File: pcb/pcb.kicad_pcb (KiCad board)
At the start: 2 copper layers, 100 x 80 mm, 20 parts, among them K1 Generic_Relay, K2 Generic_Relay, Q1 BC547, Q2 BC547

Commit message: Update optocoupler footprint and PCB with new model
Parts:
- OP1: value Optocoupler_L -> Optocoupler_Left; footprint Custom_Footprints:Optocoupler_L -> Custom_Footprints:Optocoupler_Left
- OP2: value Optocoupler_R -> Optocoupler_Right; footprint Custom_Footprints:Optocoupler_R -> Custom_Footprints:Optocoupler_Right
- moved OP2 1.60 mm to (151.2, 65.7)
- moved OP1 1.60 mm to (128.9, 65.7)
- moved R1 0.64 mm to (111.8, 59.7)
- moved R2 0.64 mm to (168.3, 59.7)
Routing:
- net Net-(OP1-LDR1): track 82.8 -> 80.5 mm
- net Net-(OP2-IN1): track 4.44 -> 5.72 mm
- net Net-(Device2-Pin_1): track 24.1 -> 25.4 mm
- net Net-(OP1-IN1): track 4.44 -> 5.71 mm
- net Net-(Device1-Pin_1): track 24.1 -> 25.4 mm
- net Net-(MCU1-D5): track 42.9 -> 43.9 mm
- net Net-(MCU1-D1): track 36.8 -> 37.8 mm
- net Net-(Device2-Pin_3): track 49.1 -> 49.8 mm
- net Net-(Device1-Pin_3): track 34.6 -> 35.2 mm

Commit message: Add PCB mounting holes
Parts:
- added REF**: MountingHole_4mm, MountingHole:MountingHole_4mm, F.Cu at (161.9, 76.2)
- added REF**: MountingHole_4mm, MountingHole:MountingHole_4mm, F.Cu at (97.2, 109.9)
- added REF**: MountingHole_4mm, MountingHole:MountingHole_4mm, F.Cu at (177.2, 118.1)
- added REF**: MountingHole_4mm, MountingHole:MountingHole_4mm, F.Cu at (118.7, 76.2)
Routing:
- net Net-(D3-K): track 146.4 -> 147.5 mm
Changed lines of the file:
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@@
     )
+  )
+  (footprint "MountingHole:MountingHole_4mm" (layer "F.Cu")
+    (at 161.925 76.2)
+    (descr "Mounting Hole 4mm, no annular")
+    (tags "mounting hole 4mm no annular")
+    (attr exclude_from_pos_files exclude_from_bom)
+    (fp_text reference "REF**" (at 0 -5) (layer "F.SilkS") hide
+        (effects (font (size 1 1) (thickness 0.15)))
+    )
+    (fp_text value "MountingHole_4mm" (at 0 5) (layer "F.Fab") hide
+        (effects (font (size 1 1) (thickness 0.15)))
+    )
+    (fp_text user "${REFERENCE}" (at 0 0) (layer "F.Fab")
+        (effects (font (size 1 1) (thickness 0.15)))
+    )
+    (fp_circle (center 0 0) (end 4 0)
+      (stroke (width 0.15) (type solid)) (fill none) (layer "Cmts.User"))
+    (fp_circle (center 0 0) (end 4.25 0)
+      (stroke (width 0.05) (type solid)) (fill none) (layer "F.CrtYd"))
+    (pad "" np_thru_hole circle (at 0 0) (size 4 4) (drill 4) (layers "F&B.Cu" "*.Mask")
+      (clearance 1))
   )
   (footprint "Resistor_THT:R_Axial_DIN0207_L6.3mm_D2.5mm_P10.16mm_Horizontal" (layer "F.Cu")
@@
       (rotate (xyz 0 0 0))
     )
+  )
+  (footprint "MountingHole:MountingHole_4mm" (layer "F.Cu")
+    (at 97.155 109.855)
+    (descr "Mounting Hole 4mm, no annular")
+    (tags "mounting hole 4mm no annular")
+    (attr exclude_from_pos_files exclude_from_bom)
+    (fp_text reference "REF**" (at 0 -5) (layer "F.SilkS") hide
+        (effects (font (size 1 1) (thickness 0.15)))
+    )
+    (fp_text value "MountingHole_4mm" (at 0 5) (layer "F.Fab") hide
+        (effects (font (size 1 1) (thickness 0.15)))
+    )
+    (fp_text user "${REFERENCE}" (at 0 0) (layer "F.Fab")
+        (effects (font (size 1 1) (thickness 0.15)))
+    )
+    (fp_circle (center 0 0) (end 4 0)
+      (stroke (width 0.15) (type solid)) (fill none) (layer "Cmts.User"))
+    (fp_circle (center 0 0) (end 4.25 0)
+      (stroke (width 0.05) (type solid)) (fill none) (layer "F.CrtYd"))
+    (pad "" np_thru_hole circle (at 0 0) (size 4 4) (drill 4) (layers "F&B.Cu" "*.Mask")
+      (clearance 1))
   )
   (footprint "Custom_Footprints:TerminalBlock_1x04" (layer "F.Cu")
@@
     )
   )
+  (footprint "MountingHole:MountingHole_4mm" (layer "F.Cu")
+    (at 177.165 118.11)
+    (descr "Mounting Hole 4mm, no annular")
+    (tags "mounting hole 4mm no annular")
+    (attr exclude_from_pos_files exclude_from_bom)
+    (fp_text reference "REF**" (at 0 -5) (layer "F.SilkS") hide
+        (effects (font (size 1 1) (thickness 0.15)))
+    )
+    (fp_text value "MountingHole_4mm" (at 0 5) (layer "F.Fab") hide
+        (effects (font (size 1 1) (thickness 0.15)))
+    )
+    (fp_text user "${REFERENCE}" (at 0 0) (layer "F.Fab")
+        (effects (font (size 1 1) (thickness 0.15)))
+    )
+    (fp_circle (center 0 0) (end 4 0)
+      (stroke (width 0.15) (type solid)) (fill none) (layer "Cmts.User"))
+    (fp_circle (center 0 0) (end 4.25 0)
+      (stroke (width 0.05) (type solid)) (fill none) (layer "F.CrtYd"))
+    (pad "" np_thru_hole circle (at 0 0) (size 4 4) (drill 4) (layers "F&B.Cu" "*.Mask")
+      (clearance 1))
+  )
   (footprint "Custom_Footprints:Optocoupler_Left" (layer "F.Cu")
     (at 128.88 65.67 90)
@@
     )
   )
+  (footprint "MountingHole:MountingHole_4mm" (layer "F.Cu")
+    (at 118.745 76.2)
+    (descr "Mounting Hole 4mm, no annular")
+    (tags "mounting hole 4mm no annular")
+    (attr exclude_from_pos_files exclude_from_bom)
+    (fp_text reference "REF**" (at 0 -5) (layer "F.SilkS") hide
+        (effects (font (size 1 1) (thickness 0.15)))
+    )
+    (fp_text value "MountingHole_4mm" (at 0 5) (layer "F.Fab") hide
+        (effects (font (size 1 1) (thickness 0.15)))
+    )
+    (fp_text user "${REFERENCE}" (at 0 0) (layer "F.Fab")
+        (effects (font (size 1 1) (thickness 0.15)))
+    )
+    (fp_circle (center 0 0) (end 4 0)
+      (stroke (width 0.15) (type solid)) (fill none) (layer "Cmts.User"))
+    (fp_circle (center 0 0) (end 4.25 0)
+      (stroke (width 0.05) (type solid)) (fill none) (layer "F.CrtYd"))
+    (pad "" np_thru_hole circle (at 0 0) (size 4 4) (drill 4) (layers "F&B.Cu" "*.Mask")
+      (clearance 1))
+  )
   (gr_rect (start 116 102) (end 165 128)
     (stroke (width 0.1) (type default)) (fill none) (layer "Dwgs.User"))
@@
   (segment (start 163.195 121.285) (end 163.195 111.125) (width 1) (layer "B.Cu") (net 1))
   (segment (start 188.595 109.22) (end 188.595 92.075) (width 1) (layer "B.Cu") (net 1))
-  (segment (start 97.25 104.87) (end 103.505 111.125) (width 1) (layer "B.Cu") (net 1))
-  (segment (start 97.25 102.52) (end 97.25 104.87) (width 1) (layer "B.Cu") (net 1))
+  (segment (start 116.84 111.125) (end 106.045 111.125) (width 1) (layer "B.Cu") (net 1))
   (segment (start 163.195 111.125) (end 186.69 111.125) (width 1) (layer "B.Cu") (net 1))
   (segment (start 186.69 111.125) (end 188.595 109.22) (width 1) (layer "B.Cu") (net 1))
   (segment (start 188.595 92.075) (end 187.04 90.52) (width 1) (layer "B.Cu") (net 1))
-  (segment (start 103.505 111.125) (end 97.155 117.475) (width 1) (layer "B.Cu") (net 1))
+  (segment (start 97.44 102.52) (end 106.045 111.125) (width 1) (layer "B.Cu") (net 1))
+  (segment (start 97.25 102.52) (end 97.44 102.52) (width 1) (layer "B.Cu") (net 1))
+  (segment (start 106.045 111.125) (end 99.695 117.475) (width 1) (layer "B.Cu") (net 1))
   (segment (start 158.115 126.365) (end 163.195 121.285) (width 1) (layer "B.Cu") (net 1))
+  (segment (start 99.695 117.475) (end 97.155 117.475) (width 1) (layer "B.Cu") (net 1))
   (segment (start 116.84 111.125) (end 163.195 111.125) (width 1) (layer "B.Cu") (net 1))
-  (segment (start 116.84 111.125) (end 103.505 111.125) (width 1) (layer "B.Cu") (net 1))
   (segment (start 187.04 90.52) (end 183.42 90.52) (width 1) (layer "B.Cu") (net 1))
   (segment (start 179.895 106.045) (end 183.42 102.52) (width 1) (layer "B.Cu") (net 2))

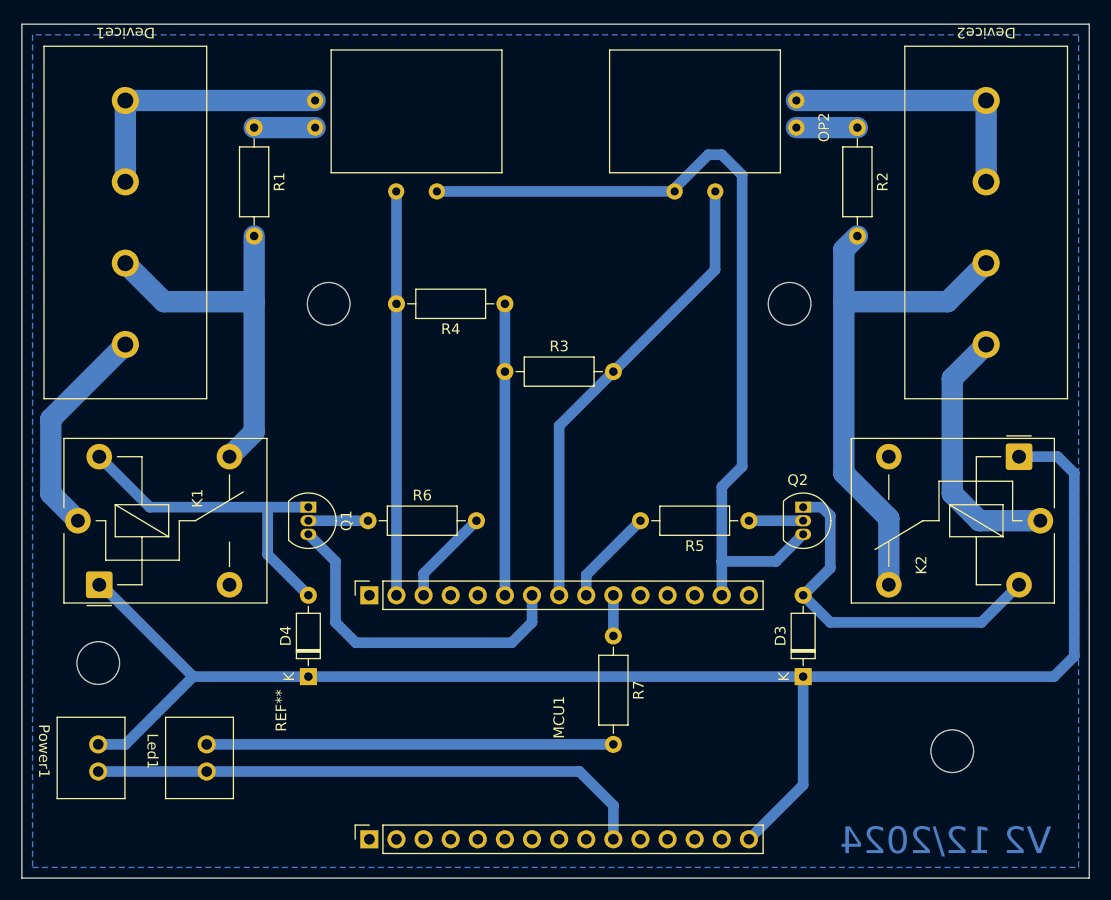
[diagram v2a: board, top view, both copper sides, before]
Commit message: Relocate PCB screw holes
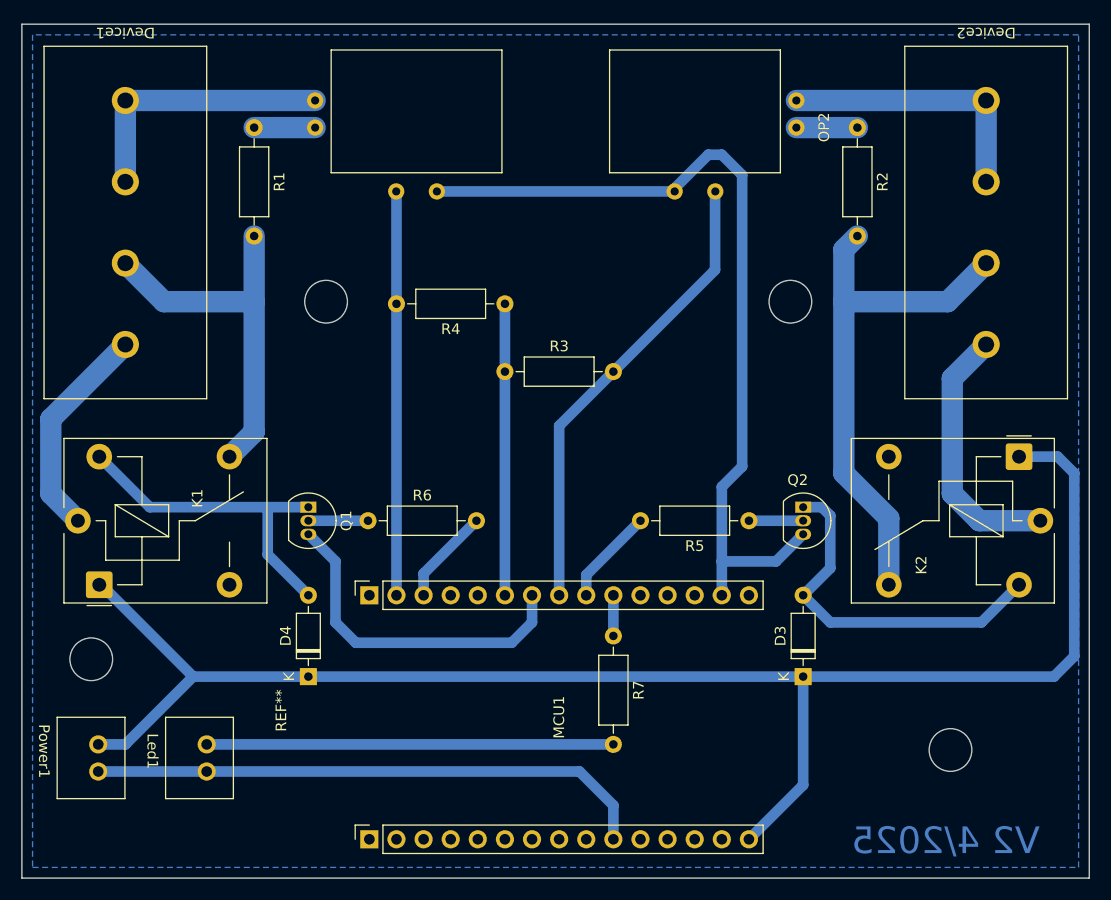
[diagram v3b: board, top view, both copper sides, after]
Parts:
- moved REF** 0.75 mm to (96.5, 109.5)
- moved REF** 0.32 mm to (118.5, 76.0)
- moved REF** 0.21 mm to (162.0, 76.0)
- moved REF** 0.20 mm to (177.0, 118.0)
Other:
- board text added: "V2 4/2025"
- board text removed: "V2 12/2024"
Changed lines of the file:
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@@
   (title_block
     (title "BombitApp")
-    (date "12/2024")
+    (date "4/2025")
     (rev "V2")
   )
@@
       (drillshape 2)
       (scaleselection 1)
-      (outputdirectory "")
+      (outputdirectory "E:/Users/Lucas/Desktop/")
     )
   )
@@
   )
   (footprint "MountingHole:MountingHole_4mm" (layer "F.Cu")
-    (at 161.925 76.2)
+    (at 162 76)
     (descr "Mounting Hole 4mm, no annular")
     (tags "mounting hole 4mm no annular")
@@
   )
   (footprint "MountingHole:MountingHole_4mm" (layer "F.Cu")
-    (at 97.155 109.855)
+    (at 96.5 109.5)
     (descr "Mounting Hole 4mm, no annular")
     (tags "mounting hole 4mm no annular")
@@
   )
   (footprint "MountingHole:MountingHole_4mm" (layer "F.Cu")
-    (at 177.165 118.11)
+    (at 177 118)
     (descr "Mounting Hole 4mm, no annular")
     (tags "mounting hole 4mm no annular")
@@
   )
   (footprint "MountingHole:MountingHole_4mm" (layer "F.Cu")
-    (at 118.745 76.2)
+    (at 118.5 76)
     (descr "Mounting Hole 4mm, no annular")
     (tags "mounting hole 4mm no annular")
@@
   (gr_line (start 190 130) (end 90 130)
     (stroke (width 0.1) (type solid)) (layer "Edge.Cuts"))
-  (gr_text "V2 12/2024" (at 176.53 126.5) (layer "B.Cu")
+  (gr_text "V2 4/2025" (at 176.53 126.5) (layer "B.Cu")
     (effects (font (size 2.5 2.5) (thickness 0.5)) (justify mirror))
   )

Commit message: Update PCB date
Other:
- board text added: "V2 8/2025"
- board text removed: "V2 4/2025"
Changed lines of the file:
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@@
   (title_block
     (title "BombitApp")
-    (date "4/2025")
+    (date "8/2025")
     (rev "V2")
   )
@@
       (drillshape 2)
       (scaleselection 1)
-      (outputdirectory "E:/Users/Lucas/Desktop/")
+      (outputdirectory "E:/Users/Lucas/Desktop/test")
     )
   )
@@
   (gr_line (start 190 130) (end 90 130)
     (stroke (width 0.1) (type solid)) (layer "Edge.Cuts"))
-  (gr_text "V2 4/2025" (at 176.53 126.5) (layer "B.Cu")
+  (gr_text "V2 8/2025" (at 176.53 126.5) (layer "B.Cu")
     (effects (font (size 2.5 2.5) (thickness 0.5)) (justify mirror))
   )
